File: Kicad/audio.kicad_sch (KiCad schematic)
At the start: 70 parts, among them J701 CD Audio In, J702 AC'97 Audio Header, J703 Line Out, U701 TLV320AIC23BPW, U702 STX-4335-5BGP-S1, Y701 12M 20pF

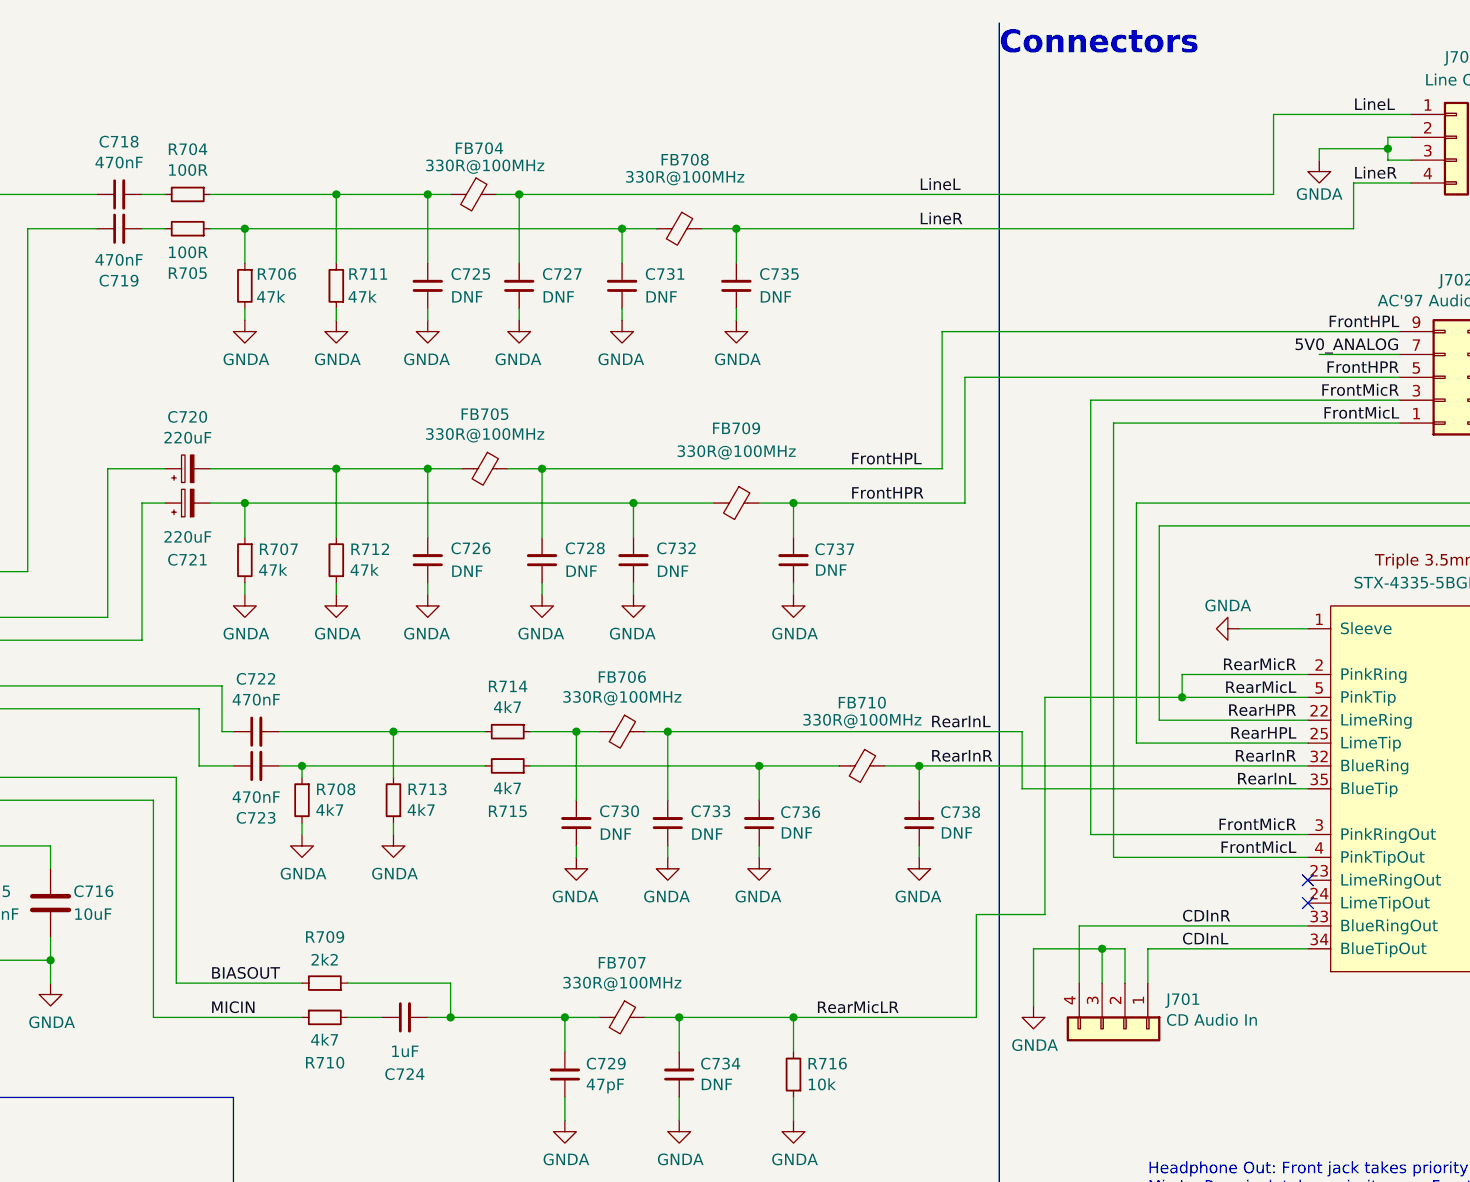
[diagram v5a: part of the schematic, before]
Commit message: LED and Switch updates.
Case LEDs are now driven by VDC and 1K. Allows higher Vf LEDs to work.
Added 6mm buttons.
Fiddled with tracking around CODEC.
Change I2S pin ordering.

Closes: #42 #60 #46
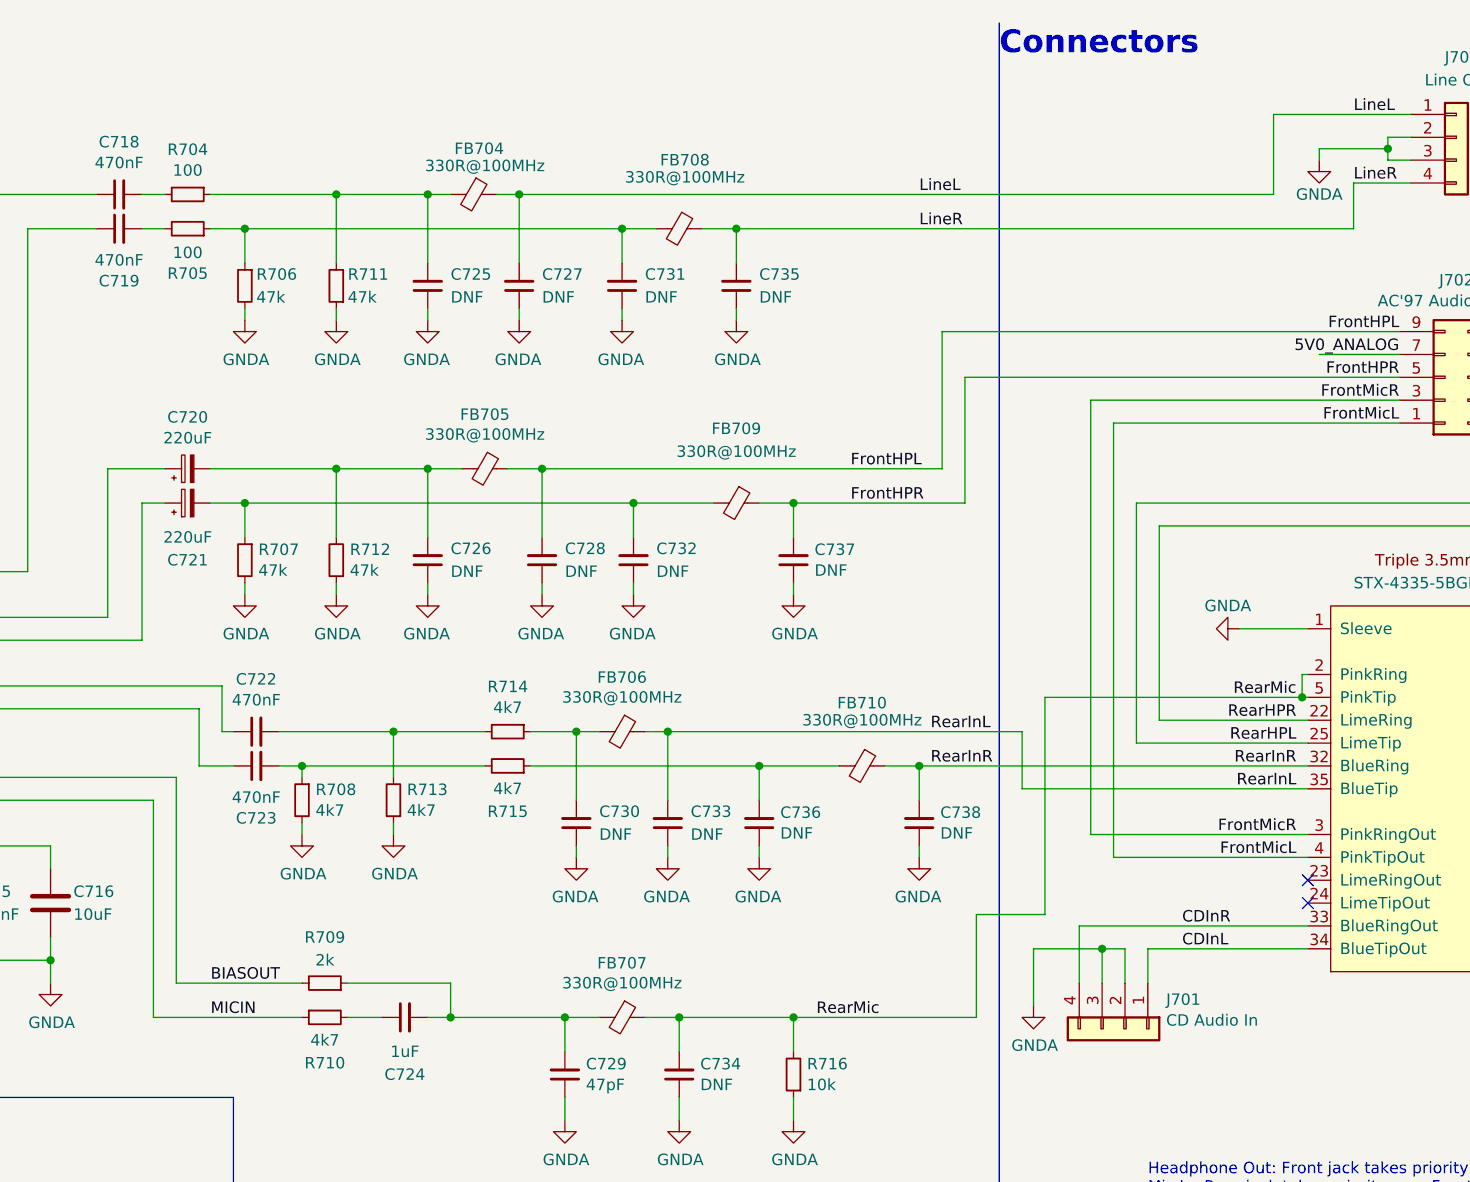
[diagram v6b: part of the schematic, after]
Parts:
- R704, R705: value 100R -> 100
- R709: value 2k2 -> 2k; Digikey RMCF0805FT2K20CT-ND -> RMCF0805FT2K00CT-ND; LCSC Part# C17520 -> C17604; MPN RMCF0805FT2K20 -> RMCF0805FT2K00
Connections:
- net RearMicL renamed RearMic
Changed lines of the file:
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@@
   (junction (at 43.18 45.72) (diameter 0) (color 0 0 0 0)
   )
+  (junction (at 240.665 87.63) (diameter 0) (color 0 0 0 0)
+  )
   (junction (at 123.19 66.04) (diameter 0) (color 0 0 0 0)
   )
@@
   (junction (at 171.45 123.19) (diameter 0) (color 0 0 0 0)
   )
-  (junction (at 227.33 87.63) (diameter 0) (color 0 0 0 0)
-  )
   (junction (at 180.34 95.25) (diameter 0) (color 0 0 0 0)
   )
@@
     (stroke (width 0) (type default) (color 0 0 0 0))
   )
+  (wire (pts (xy 240.665 87.63) (xy 241.3 87.63))
+    (stroke (width 0) (type default) (color 0 0 0 0))
+  )
   (wire (pts (xy 217.17 54.61) (xy 251.46 54.61))
     (stroke (width 0) (type default) (color 0 0 0 0))
@@
     (stroke (width 0) (type default) (color 0 0 0 0))
   )
+  (wire (pts (xy 212.09 87.63) (xy 240.665 87.63))
+    (stroke (width 0) (type default) (color 0 0 0 0))
+  )
   (wire (pts (xy 224.79 90.17) (xy 224.79 68.58))
     (stroke (width 0) (type default) (color 0 0 0 0))
@@
     (stroke (width 0) (type default) (color 0 0 0 0))
   )
-  (wire (pts (xy 227.33 87.63) (xy 241.3 87.63))
-    (stroke (width 0) (type default) (color 0 0 0 0))
-  )
   (wire (pts (xy 166.37 74.93) (xy 166.37 76.2))
     (stroke (width 0) (type default) (color 0 0 0 0))
@@
     (stroke (width 0) (type default) (color 0 0 0 0))
   )
-  (wire (pts (xy 227.33 85.09) (xy 227.33 87.63))
+  (wire (pts (xy 240.665 85.09) (xy 240.665 87.63))
     (stroke (width 0) (type default) (color 0 0 0 0))
   )
@@
     (stroke (width 0) (type default) (color 0 0 0 0))
   )
-  (wire (pts (xy 212.09 87.63) (xy 227.33 87.63))
-    (stroke (width 0) (type default) (color 0 0 0 0))
-  )
   (wire (pts (xy 93.98 31.75) (xy 93.98 71.12))
     (stroke (width 0) (type default) (color 0 0 0 0))
@@
     (stroke (width 0) (type default) (color 0 0 0 0))
   )
-  (wire (pts (xy 227.33 85.09) (xy 241.3 85.09))
+  (wire (pts (xy 240.665 85.09) (xy 241.3 85.09))
     (stroke (width 0) (type default) (color 0 0 0 0))
   )
@@
     (effects (font (size 1.27 1.27)) (justify left bottom))
   )
-  (label "RearMicLR" (at 186.69 123.19 0)
+  (label "RearMic" (at 186.69 123.19 0)
     (effects (font (size 1.27 1.27)) (justify left bottom))
   )
@@
     (effects (font (size 1.27 1.27)) (justify right bottom))
   )
-  (label "RearMicR" (at 240.03 85.09 180)
+  (label "RearMic" (at 240.03 87.63 180)
     (effects (font (size 1.27 1.27)) (justify right bottom))
   )
@@
     (effects (font (size 1.27 1.27)) (justify left bottom))
   )
-  (label "RearMicL" (at 240.03 87.63 180)
-    (effects (font (size 1.27 1.27)) (justify right bottom))
-  )
   (label "BIASOUT" (at 119.38 119.38 0)
     (effects (font (size 1.27 1.27)) (justify left bottom))
@@
     (in_bom yes) (on_board yes)
     (property "Reference" "R704" (id 0) (at 116.84 26.7716 90))
-    (property "Value" "100R" (id 1) (at 116.84 29.083 90))
+    (property "Value" "100" (id 1) (at 116.84 29.083 90))
     (property "Footprint" "Resistor_SMD:R_0805_2012Metric_Pad1.20x1.40mm_HandSolder" (id 2) (at 116.84 31.75 0)
       (effects (font (size 1.27 1.27)) hide)
@@
     (in_bom yes) (on_board yes)
     (property "Reference" "R705" (id 0) (at 116.84 40.5384 90))
-    (property "Value" "100R" (id 1) (at 116.84 38.227 90))
+    (property "Value" "100" (id 1) (at 116.84 38.227 90))
     (property "Footprint" "Resistor_SMD:R_0805_2012Metric_Pad1.20x1.40mm_HandSolder" (id 2) (at 116.84 35.56 0)
       (effects (font (size 1.27 1.27)) hide)
@@
     (in_bom yes) (on_board yes)
     (property "Reference" "R709" (id 0) (at 132.08 114.3 90))
-    (property "Value" "2k2" (id 1) (at 132.08 116.84 90))
+    (property "Value" "2k" (id 1) (at 132.08 116.84 90))
     (property "Footprint" "Resistor_SMD:R_0805_2012Metric_Pad1.20x1.40mm_HandSolder" (id 2) (at 132.08 119.38 0)
       (effects (font (size 1.27 1.27)) hide)
@@
       (effects (font (size 1.27 1.27)) hide)
     )
-    (property "Digikey" "RMCF0805FT2K20CT-ND" (id 5) (at 132.08 119.38 0)
+    (property "Digikey" "RMCF0805FT2K00CT-ND" (id 5) (at 132.08 119.38 0)
       (effects (font (size 1.27 1.27)) hide)
     )
-    (property "MPN" "RMCF0805FT2K20" (id 6) (at 132.08 119.38 0)
+    (property "MPN" "RMCF0805FT2K00" (id 6) (at 132.08 119.38 0)
       (effects (font (size 1.27 1.27)) hide)
     )
@@
       (effects (font (size 1.27 1.27)) hide)
     )
-    (property "LCSC Part#" "C17520" (id 8) (at 132.08 119.38 0)
+    (property "LCSC Part#" "C17604" (id 8) (at 132.08 119.38 0)
       (effects (font (size 1.27 1.27)) hide)
     )

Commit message: Cleaned up the part numbers.
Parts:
- C701, C705: Digikey 1276-1047-1-ND -> (none); JLCPCB Collection (none) -> Basic; Voltage 16V -> 50V
- C702, C703, C704, C706, C708, C709, C713, C716: Digikey 490-3886-1-ND -> (none); JLCPCB Collection (none) -> Basic; MPN GRM21BR61C106KE15L -> CL21A106KAYNNNE; Manufacturer Murata -> Samsung; Mouser 81-GRM21BR61C106KE15 -> (none); Voltage 10V -> 25V
- C707, C710, C711, C712, C715: Digikey 399-C0805C104M5RAC7800CT-ND -> (none); JLCPCB Collection (none) -> Basic; MPN C0805C104M5RACTU -> CC0805KRX7R9BB104; Manufacturer Kemet -> Yageo; Mouser 80-C0805C104M5R -> (none); Tolerance X5R -> X7R; Voltage 10V -> 50V
- C714, C717: Digikey 490-3886-1-ND -> (none); JLCPCB Collection (none) -> Basic; MPN GRM21BR61C106KE15L -> CL21A106KAYNNNE; Manufacturer Murata -> Samsung; Mouser 81-GRM21BR61C106KE15 -> (none); Voltage 16V -> 25V
- C718, C719, C722, C723: Digikey 445-173276-1-ND -> (none); JLCPCB Collection (none) -> Basic; Manufacturer TDK -> Samsung; Mouser 810-FG18X7R1H474KRT6 -> (none); Tolerance X5R -> X7R; Voltage 6.3V -> 50V
- C724: Digikey 311-1456-1-ND -> (none); JLCPCB Collection (none) -> Basic; MPN CC0805KKX7R8BB105 -> CL21B105KBFNNNE; Manufacturer Yageo -> Samsung; Mouser 603-CC805KKX7R8BB105 -> (none); Tolerance X5R -> X7R; Voltage 6.3V -> 50V
- C729: Digikey 1276-1156-1-ND -> (none); JLCPCB Collection (none) -> Basic; Voltage 6.3V -> 50V
- FB701, FB702, FB703, FB704, FB705, FB706, FB707, FB708, FB709, FB710: Digikey 490-5988-6-ND -> (none); JLCPCB Collection (none) -> Basic; MPN BLM21PG331SN1D -> GZ2012D601TF; Manufacturer Murata -> Sunlord; Mouser 81-BLM21P331SG -> (none); Tolerance 1.5A -> 25%
- J701: value CD Audio In -> Conn_01x04
- J702: value AC'97 Audio Header -> Conn_02x05
- J703: value Line Out -> Conn_01x04
- R701, R702, R703: Digikey RMCF0805FT2R20CT-ND -> (none); JLCPCB Collection (none) -> Basic; MPN RMCF0805FT2R20 -> 0805W8F220KT5E; Manufacturer Stackpole -> Uniroyal
- R704, R705: Digikey RMCF0805FT100RCT-ND -> (none); JLCPCB Collection (none) -> Basic; MPN RMCF0805FT100R -> 0805W8F1000T5E; Manufacturer Stackpole -> Uniroyal
- R706, R707, R711, R712: Digikey RMCF0805FT47K5CT-ND -> (none); JLCPCB Collection (none) -> Basic; MPN RMCF0805FT47K5 -> 0805W8F4702T5E; Manufacturer Stackpole -> Uniroyal
- R708, R710, R713, R714, R715: Digikey RMCF0805FT4K70CT-ND -> (none); JLCPCB Collection (none) -> Basic; MPN RMCF0805FT4K70 -> 0805W8F4701T5E; Manufacturer Stackpole -> Uniroyal
- R709: Digikey RMCF0805FT2K00CT-ND -> (none); JLCPCB Collection (none) -> Basic; MPN RMCF0805FT2K00 -> 0805W8F2001T5E; Manufacturer Stackpole -> Uniroyal
- R716: Digikey RMCF0805FT10K0CT-ND -> (none); JLCPCB Collection (none) -> Basic; MPN RMCF0805FT10K0 -> 0805W8F1002T5E; Manufacturer Stackpole -> Uniroyal
- U701: Digikey 296-26817-1-ND -> (none); JLCPCB Collection (none) -> Extended; Mouser 595-TLV320AIC23BPW -> (none)
- Y701: Digikey 535-9116-1-ND -> (none); JLCPCB Collection (none) -> Extended; MPN ABM3B-12.000MHZ-B2-T -> 7A12000009; Manufacturer Abracon -> TXC; Mouser 815-ABM3B-12-B2 -> (none)
